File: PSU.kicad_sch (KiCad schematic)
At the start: 86 parts, among them J17 Barrel_Jack_Switch, J18 USB_C_Receptacle_USB2.0_16P, J22 Conn_02x04_Counter_Clockwise, Q5 2N7002, Q6 2N7002, Q7 AON7262E, Q8 2N7002, SW1 SW_Push, SW2 SW_Push, U13 TL431DBZ, U14 CH224K, U15 LM2734X, U16 LM2734X

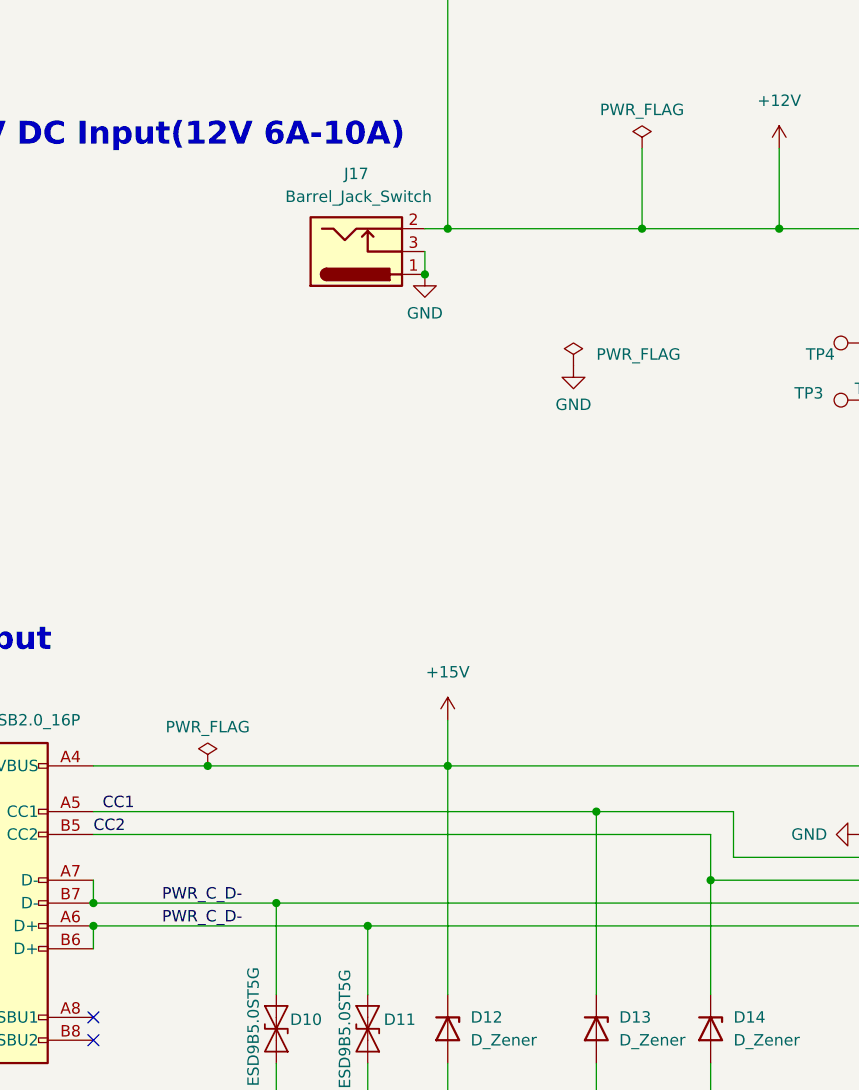
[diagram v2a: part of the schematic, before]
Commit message: Started the power circuit USB power finished and barrel jack started. Flipped barrel jack symbol in schematic sheet and added 12v planes
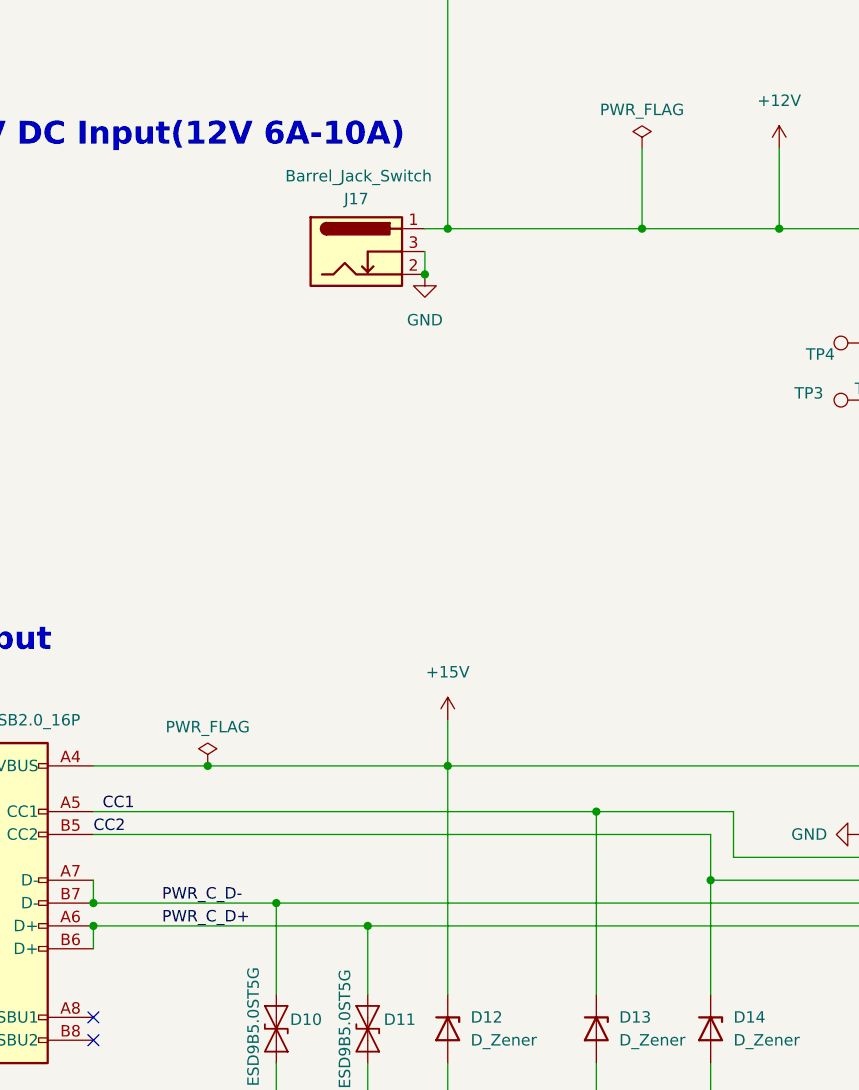
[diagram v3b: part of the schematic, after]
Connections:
- net +12V: now also J17.1; no longer J17.2
- net GND: now also J17.2; no longer J17.1
- net PWR_C_D-: no longer D11.2 (A2), J18.A6 (D+), J18.B6 (D+), U14.4 (DP)
- new net PWR_C_D+: D11.2 (A2), J18.A6 (D+), J18.B6 (D+), U14.4 (DP)
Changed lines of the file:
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@@
 	)
 	(junction
-		(at 110.49 193.04)
-		(diameter 0)
-		(color 0 0 0 0)
-	)
-	(junction
 		(at 398.78 210.82)
 		(diameter 0)
@@
 	)
 	(junction
-		(at 107.95 198.12)
-		(diameter 0)
-		(color 0 0 0 0)
-	)
-	(junction
 		(at 284.48 71.12)
 		(diameter 0)
@@
 	)
 	(junction
+		(at 110.49 193.04)
+		(diameter 0)
+		(color 0 0 0 0)
+	)
+	(junction
 		(at 363.22 355.6)
 		(diameter 0)
@@
 	)
 	(junction
+		(at 107.95 198.12)
+		(diameter 0)
+		(color 0 0 0 0)
+	)
+	(junction
 		(at 452.12 271.78)
 		(diameter 0)
@@
 	(wire
 		(pts
+			(xy 107.95 195.58) (xy 107.95 198.12)
+		)
+		(stroke
+			(width 0)
+			(type default)
+		)
+	)
+	(wire
+		(pts
 			(xy 302.26 78.74) (xy 302.26 71.12)
 		)
@@
 	(wire
 		(pts
-			(xy 107.95 193.04) (xy 110.49 193.04)
-		)
-		(stroke
-			(width 0)
-			(type default)
-		)
-	)
-	(wire
-		(pts
 			(xy 232.41 162.56) (xy 208.28 162.56)
 		)
@@
 	(wire
 		(pts
-			(xy 107.95 195.58) (xy 107.95 198.12)
-		)
-		(stroke
-			(width 0)
-			(type default)
-		)
-	)
-	(wire
-		(pts
 			(xy 294.64 355.6) (xy 294.64 363.22)
 		)
@@
 	(wire
 		(pts
+			(xy 107.95 193.04) (xy 110.49 193.04)
+		)
+		(stroke
+			(width 0)
+			(type default)
+		)
+	)
+	(wire
+		(pts
 			(xy 127 285.75) (xy 127 294.64)
 		)
@@
 		)
 	)
-	(label "PWR_C_D-"
+	(label "PWR_C_D+"
 		(at 78.74 270.51 0)
 		(effects
@@
 		(lib_id "Connector:Barrel_Jack_Switch")
 		(at 100.33 195.58 0)
-		(mirror x)
 		(unit 1)
 		(body_style 1)
@@
 		(dnp no)
 		(property "Reference" "J17"
-			(at 100.33 186.944 0)
+			(at 100.33 189.738 0)
 			(show_name no)
 			(do_not_autoplace no)
@@
 		)
 		(property "Value" "Barrel_Jack_Switch"
-			(at 100.584 189.484 0)
+			(at 100.584 187.198 0)
 			(show_name no)
 			(do_not_autoplace no)
@@
 		)
 		(property "Footprint" "A_HDJ_Library:DC_Jack_DC007B_30V_10A"
-			(at 101.6 194.564 0)
+			(at 101.6 196.596 0)
 			(hide yes)
 			(show_name no)
@@
 		)
 		(property "Datasheet" ""
-			(at 101.6 194.564 0)
+			(at 101.6 196.596 0)
 			(hide yes)
 			(show_name no)
@@
 	(symbol
 		(lib_id "power:GND")
-		(at 124.46 208.28 0)
-		(unit 1)
-		(body_style 1)
-		(exclude_from_sim no)
-		(in_bom yes)
-		(on_board yes)
-		(in_pos_files yes)
-		(dnp no)
-		(fields_autoplaced yes)
-		(property "Reference" "#PWR096"
-			(at 124.46 214.63 0)
-			(hide yes)
-			(show_name no)
-			(do_not_autoplace no)
-			(effects
-				(font
-					(size 1.27 1.27)
-				)
-			)
-		)
-		(property "Value" "GND"
-			(at 124.46 212.598 0)
-			(show_name no)
-			(do_not_autoplace no)
-			(effects
-				(font
-					(size 1.27 1.27)
-				)
-			)
-		)
-		(property "Footprint" ""
-			(at 124.46 208.28 0)
-			(hide yes)
-			(show_name no)
-			(do_not_autoplace no)
-			(effects
-				(font
-					(size 1.27 1.27)
-				)
-			)
-		)
-		(property "Datasheet" ""
-			(at 124.46 208.28 0)
-			(hide yes)
-			(show_name no)
-			(do_not_autoplace no)
-			(effects
-				(font
-					(size 1.27 1.27)
-				)
-			)
-		)
-		(property "Description" "Power symbol creates a global label with name \"GND\" , ground"
-			(at 124.46 208.28 0)
-			(hide yes)
-			(show_name no)
-			(do_not_autoplace no)
-			(effects
-				(font
-					(size 1.27 1.27)
-				)
-			)
-		)
-		(pin "1"
-		)
-		(instances
-			(project "Carrier_Board"
-				(path "/e768274e-12f3-4f83-96f6-abb7638e0bc1/a1e78f2f-f14b-4628-9612-5b4e596f5f9f"
-					(reference "#PWR096")
-					(unit 1)
-				)
-			)
-		)
-	)
-	(symbol
-		(lib_id "power:GND")
 		(at 312.42 181.61 0)
 		(unit 1)
@@
 	)
 	(symbol
+		(lib_id "power:GND")
+		(at 107.95 198.12 0)
+		(unit 1)
+		(body_style 1)
+		(exclude_from_sim no)
+		(in_bom yes)
+		(on_board yes)
+		(in_pos_files yes)
+		(dnp no)
+		(fields_autoplaced yes)
+		(property "Reference" "#PWR0208"
+			(at 107.95 204.47 0)
+			(hide yes)
+			(show_name no)
+			(do_not_autoplace no)
+			(effects
+				(font
+					(size 1.27 1.27)
+				)
+			)
+		)
+		(property "Value" "GND"
+			(at 107.95 203.2 0)
+			(show_name no)
+			(do_not_autoplace no)
+			(effects
+				(font
+					(size 1.27 1.27)
+				)
+			)
+		)
+		(property "Footprint" ""
+			(at 107.95 198.12 0)
+			(hide yes)
+			(show_name no)
+			(do_not_autoplace no)
+			(effects
+				(font
+					(size 1.27 1.27)
+				)
+			)
+		)
+		(property "Datasheet" ""
+			(at 107.95 198.12 0)
+			(hide yes)
+			(show_name no)
+			(do_not_autoplace no)
+			(effects
+				(font
+					(size 1.27 1.27)
+				)
+			)
+		)
+		(property "Description" "Power symbol creates a global label with name \"GND\" , ground"
+			(at 107.95 198.12 0)
+			(hide yes)
+			(show_name no)
+			(do_not_autoplace no)
+			(effects
+				(font
+					(size 1.27 1.27)
+				)
+			)
+		)
+		(pin "1"
+		)
+		(instances
+			(project "Carrier_Board"
+				(path "/e768274e-12f3-4f83-96f6-abb7638e0bc1/a1e78f2f-f14b-4628-9612-5b4e596f5f9f"
+					(reference "#PWR0208")
+					(unit 1)
+				)
+			)
+		)
+	)
+	(symbol
 		(lib_id "Device:C_Small")
 		(at 431.8 208.28 0)
@@
 	(symbol
 		(lib_id "power:GND")
-		(at 107.95 198.12 0)
-		(unit 1)
-		(body_style 1)
-		(exclude_from_sim no)
-		(in_bom yes)
-		(on_board yes)
-		(in_pos_files yes)
-		(dnp no)
-		(fields_autoplaced yes)
-		(property "Reference" "#PWR094"
-			(at 107.95 204.47 0)
-			(hide yes)
-			(show_name no)
-			(do_not_autoplace no)
-			(effects
-				(font
-					(size 1.27 1.27)
-				)
-			)
-		)
-		(property "Value" "GND"
-			(at 107.95 202.438 0)
-			(show_name no)
-			(do_not_autoplace no)
-			(effects
-				(font
-					(size 1.27 1.27)
-				)
-			)
-		)
-		(property "Footprint" ""
-			(at 107.95 198.12 0)
-			(hide yes)
-			(show_name no)
-			(do_not_autoplace no)
-			(effects
-				(font
-					(size 1.27 1.27)
-				)
-			)
-		)
-		(property "Datasheet" ""
-			(at 107.95 198.12 0)
-			(hide yes)
-			(show_name no)
-			(do_not_autoplace no)
-			(effects
-				(font
-					(size 1.27 1.27)
-				)
-			)
-		)
-		(property "Description" "Power symbol creates a global label with name \"GND\" , ground"
-			(at 107.95 198.12 0)
-			(hide yes)
-			(show_name no)
-			(do_not_autoplace no)
-			(effects
-				(font
-					(size 1.27 1.27)
-				)
-			)
-		)
-		(pin "1"
-		)
-		(instances
-			(project "Carrier_Board"
-				(path "/e768274e-12f3-4f83-96f6-abb7638e0bc1/a1e78f2f-f14b-4628-9612-5b4e596f5f9f"
-					(reference "#PWR094")
-					(unit 1)
-				)
-			)
-		)
-	)
-	(symbol
-		(lib_id "power:GND")
 		(at 201.93 270.51 90)
 		(unit 1)
@@
 					(unit 1)
 				)
-			)
-		)
-	)
-	(symbol
-		(lib_id "power:PWR_FLAG")
-		(at 124.46 208.28 0)
-		(unit 1)
-		(body_style 1)
-		(exclude_from_sim no)
-		(in_bom yes)
-		(on_board yes)
-		(in_pos_files yes)
-		(dnp no)
-		(fields_autoplaced yes)
-		(property "Reference" "#FLG080"
-			(at 124.46 206.375 0)
-			(hide yes)
-			(show_name no)
-			(do_not_autoplace no)
-			(effects
-				(font
-					(size 1.27 1.27)
-				)
-			)
-		)
-		(property "Value" "PWR_FLAG"
-			(at 127 207.0099 0)
-			(show_name no)
-			(do_not_autoplace no)
-			(effects
-				(font
-					(size 1.27 1.27)
-				)
-				(justify left)
-			)
-		)
-		(property "Footprint" ""
-			(at 124.46 208.28 0)
-			(hide yes)
-			(show_name no)
-			(do_not_autoplace no)
-			(effects
-				(font
-					(size 1.27 1.27)
-				)
-			)
-		)
-		(property "Datasheet" ""
-			(at 124.46 208.28 0)
-			(hide yes)
-			(show_name no)
-			(do_not_autoplace no)
-			(effects
-				(font
-					(size 1.27 1.27)
-				)
-			)
-		)
-		(property "Description" "Special symbol for telling ERC where power comes from"
-			(at 124.46 208.28 0)
-			(hide yes)
-			(show_name no)
-			(do_not_autoplace no)
-			(effects
-				(font
-					(size 1.27 1.27)
-				)
-			)
-		)
-		(pin "1"
-		)
-		(instances
-			(project "Carrier_Board"
-				(path "/e768274e-12f3-4f83-96f6-abb7638e0bc1/a1e78f2f-f14b-4628-9612-5b4e596f5f9f"
-					(reference "#FLG080")
-					(unit 1)
-				)

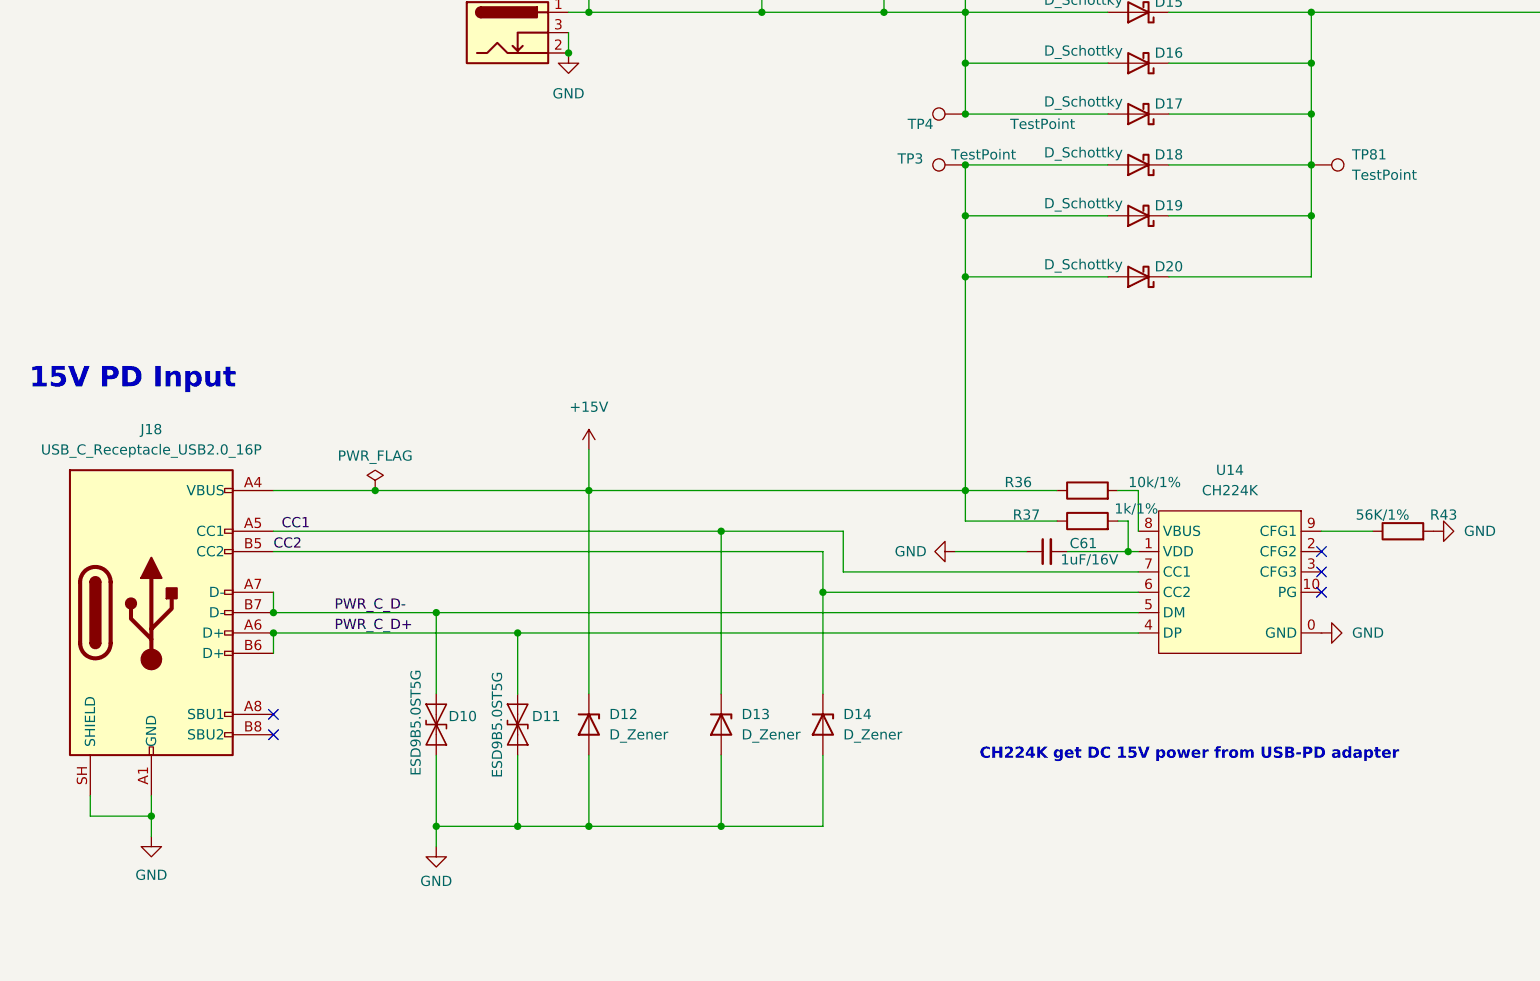
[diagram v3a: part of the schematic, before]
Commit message: 18:47 halfway through barrel jack implementation some layout components are not entirely accurate yet. fix during routing and also coirrected the footprints of U15 and U16
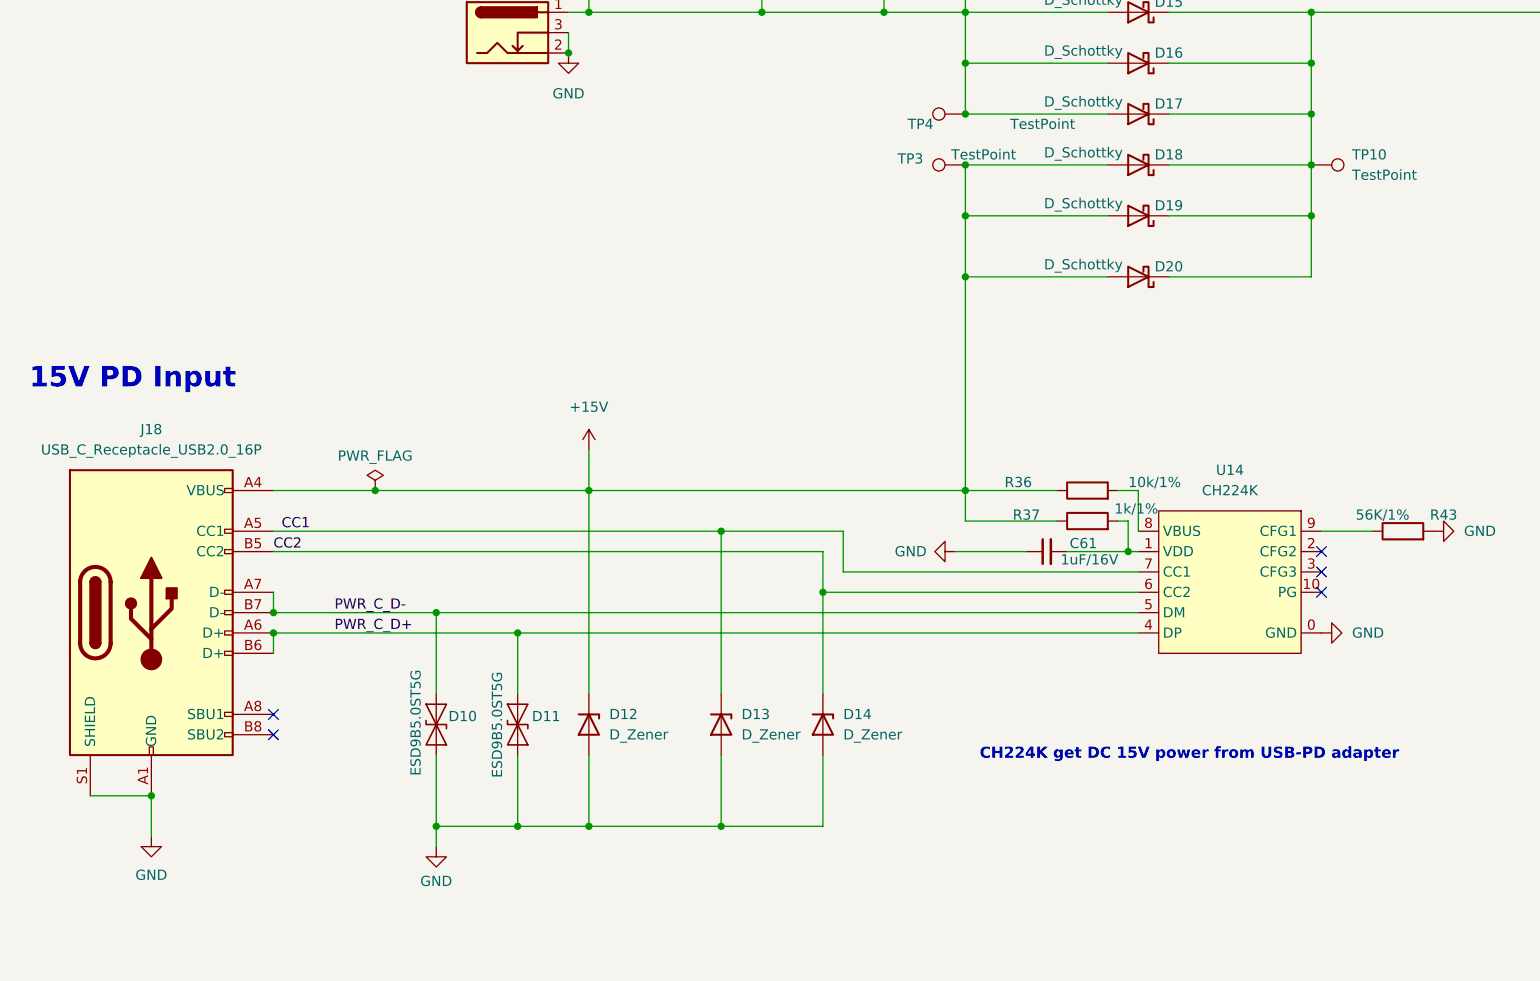
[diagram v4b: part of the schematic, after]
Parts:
- U15, U16: footprint Package_TO_SOT_SMD:TSOT-23 -> A_HDJ_Library:TSOT-23-6
- renumbered TP81 to TP10
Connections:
- net GND: now also J18.S1 (SHIELD); no longer J18.SH (SHIELD)
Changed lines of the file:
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@@
 	)
 	(junction
+		(at 55.88 290.83)
+		(diameter 0)
+		(color 0 0 0 0)
+	)
+	(junction
 		(at 200.66 193.04)
 		(diameter 0)
@@
 	)
 	(junction
-		(at 55.88 293.37)
-		(diameter 0)
-		(color 0 0 0 0)
-	)
-	(junction
 		(at 157.48 193.04)
 		(diameter 0)
@@
 	(wire
 		(pts
-			(xy 55.88 293.37) (xy 55.88 295.91)
-		)
-		(stroke
-			(width 0)
-			(type default)
-		)
-	)
-	(wire
-		(pts
 			(xy 71.12 270.51) (xy 101.6 270.51)
 		)
@@
 	(wire
 		(pts
+			(xy 48.26 290.83) (xy 55.88 290.83)
+		)
+		(stroke
+			(width 0)
+			(type default)
+		)
+	)
+	(wire
+		(pts
 			(xy 284.48 170.18) (xy 284.48 172.72)
 		)
@@
 	(wire
 		(pts
-			(xy 48.26 290.83) (xy 48.26 293.37)
-		)
-		(stroke
-			(width 0)
-			(type default)
-		)
-	)
-	(wire
-		(pts
 			(xy 259.08 81.28) (xy 259.08 83.82)
 		)
@@
 	(wire
 		(pts
-			(xy 48.26 293.37) (xy 55.88 293.37)
-		)
-		(stroke
-			(width 0)
-			(type default)
-		)
-	)
-	(wire
-		(pts
 			(xy 284.48 73.66) (xy 284.48 76.2)
 		)
@@
 	(wire
 		(pts
-			(xy 55.88 290.83) (xy 55.88 293.37)
-		)
-		(stroke
-			(width 0)
-			(type default)
-		)
-	)
-	(wire
-		(pts
 			(xy 431.8 271.78) (xy 416.56 271.78)
 		)
@@
 	(wire
 		(pts
+			(xy 55.88 290.83) (xy 55.88 295.91)
+		)
+		(stroke
+			(width 0)
+			(type default)
+		)
+	)
+	(wire
+		(pts
 			(xy 398.78 210.82) (xy 398.78 214.63)
 		)
@@
 			)
 		)
-		(property "Footprint" "Package_TO_SOT_SMD:TSOT-23"
+		(property "Footprint" "A_HDJ_Library:TSOT-23-6"
 			(at 346.075 247.65 0)
 			(hide yes)
@@
 		(dnp no)
 		(fields_autoplaced yes)
-		(property "Reference" "TP81"
+		(property "Reference" "TP10"
 			(at 205.74 210.8199 90)
 			(show_name no)
@@
 			)
 		)
+		(property "Purpose" ""
+			(at 200.66 212.09 0)
+			(show_name no)
+			(do_not_autoplace no)
+			(effects
+				(font
+					(size 1.27 1.27)
+				)
+			)
+		)
 		(pin "1"
 		)
@@
 			(project "Carrier_Board"
 				(path "/e768274e-12f3-4f83-96f6-abb7638e0bc1/a1e78f2f-f14b-4628-9612-5b4e596f5f9f"
-					(reference "TP81")
+					(reference "TP10")
 					(unit 1)
 				)
@@
 		(pin "B6"
 		)
-		(pin "SH"
+		(pin "S1"
 		)
 		(pin "B5"
@@
 			)
 		)
-		(property "Footprint" "Package_TO_SOT_SMD:TSOT-23"
+		(property "Footprint" "A_HDJ_Library:TSOT-23-6"
 			(at 346.075 201.93 0)
 			(hide yes)
